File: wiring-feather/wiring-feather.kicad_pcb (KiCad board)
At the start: 2 copper layers, 1 part

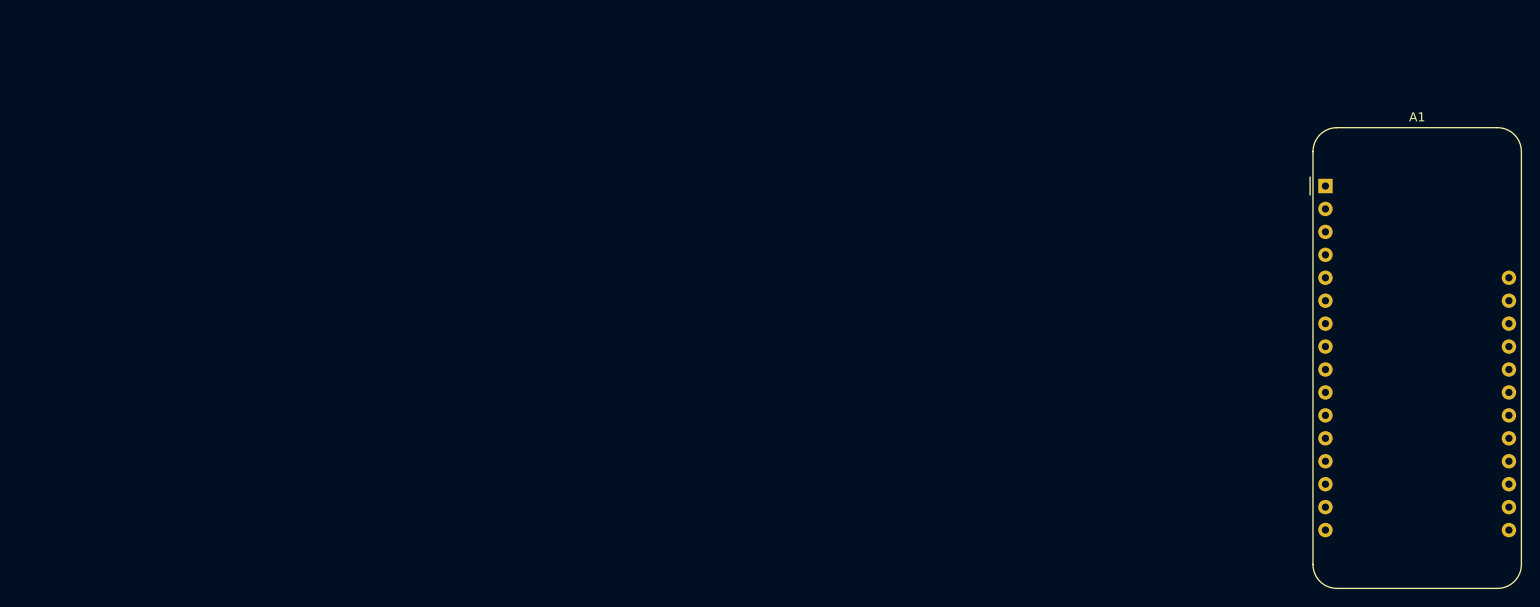
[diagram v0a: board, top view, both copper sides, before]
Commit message: Created footprint for components
All components have footprints, approx for the IMU, auto placed them on the PCB
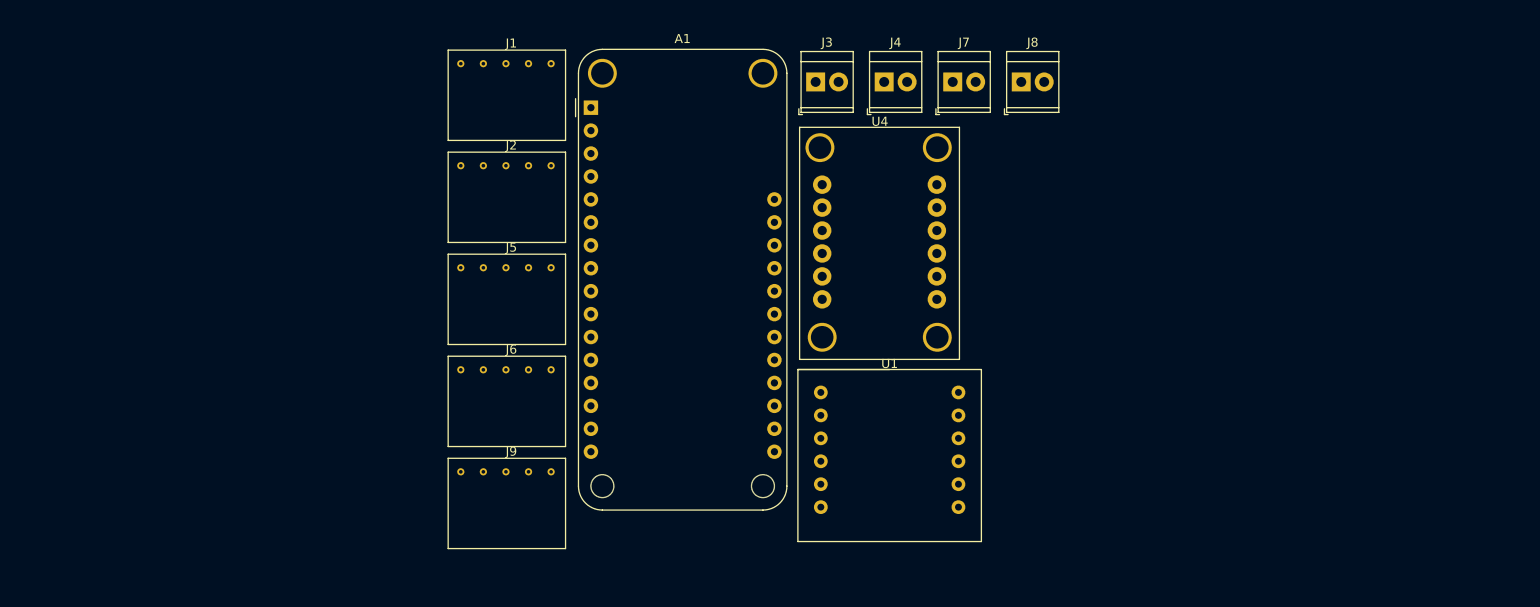
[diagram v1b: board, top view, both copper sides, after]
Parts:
- added J1: M Battery 1, 380_footprint-lib:JST_breakout, F.Cu at (118.8, 66.2)
- added J2: M Battery 1, 380_footprint-lib:JST_breakout, F.Cu at (118.8, 77.5)
- added J3: Screw_Terminal_01x02, 380_footprint-lib:Screw_terminal_TE_Connectivity, F.Cu at (159.4, 69.8)
- added J4: Screw_Terminal_01x02, 380_footprint-lib:Screw_terminal_TE_Connectivity, F.Cu at (167.0, 69.8)
- added J5: JST Breakout Board, 380_footprint-lib:JST_breakout, F.Cu at (118.8, 88.8)
- added J6: JST Breakout Board, 380_footprint-lib:JST_breakout, F.Cu at (118.8, 100.1)
- added J7: Screw_Terminal_01x02, 380_footprint-lib:Screw_terminal_TE_Connectivity, F.Cu at (174.6, 69.8)
- added J8: Screw_Terminal_01x02, 380_footprint-lib:Screw_terminal_TE_Connectivity, F.Cu at (182.2, 69.8)
- added J9: JST Breakout Board, 380_footprint-lib:JST_breakout, F.Cu at (118.8, 111.4)
- added U1: TB6612FNG-Breakout, 380_footprint-lib:DRI0044, F.Cu at (167.6, 104.1)
- added U4: ICM-20948-Adafruit, 380_footprint-lib:ICM-20948, F.Cu at (157.7, 74.8)
- A1: footprint Module:Adafruit_Feather -> 380_footprint-lib:Adafruit_Feather_M0_Adalogger
- moved A1 81.8 mm to (134.6, 72.6)

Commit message: made rough pcb
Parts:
- added D1: D, Connector_PinHeader_2.54mm:PinHeader_1x02_P2.54mm_Vertical, F.Cu at (119.4, 83.8)
- added REF**: MountingHole_2.2mm_M2, MountingHole:MountingHole_2.2mm_M2, F.Cu at (188.0, 118.1)
- added REF**: MountingHole_2.2mm_M2, MountingHole:MountingHole_2.2mm_M2, F.Cu at (102.9, 69.8)
- added REF**: MountingHole_2.2mm_M2, MountingHole:MountingHole_2.2mm_M2, F.Cu at (188.0, 69.8)
- added REF**: MountingHole_2.2mm_M2, MountingHole:MountingHole_2.2mm_M2, F.Cu at (102.9, 118.7)
- J1, J2: footprint 380_footprint-lib:JST_breakout -> Connector_JST:JST_XH_S2B-XH-A_1x02_P2.50mm_Horizontal
- moved J7 73.9 mm to (104.1, 92.1), turned to -90 degrees
- moved J4 65.2 mm to (104.1, 87.0), turned to 90 degrees
- moved U1 34.3 mm to (168.9, 69.8)
- moved J3 33.0 mm to (185.4, 90.2), turned to -90 degrees
- moved J8 29.5 mm to (185.4, 99.1), turned to -90 degrees
- moved J9 22.8 mm to (115.5, 88.9)
- moved J6 18.9 mm to (100.3, 104.1)
- moved J5 15.6 mm to (115.5, 104.1)
- moved U4 15.5 mm to (160.2, 90.1)
- moved J1 12.9 mm to (125.7, 77.1), turned to 180 degrees
- moved J2 3.23 mm to (115.5, 77.1), turned to 180 degrees
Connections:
- A1 pad 19: /PWM-M1 -> /RESET
- A1 pad 20: /DIR1-M1 -> /DIR1-M2
- A1 pad 23: /DIR1-M2 -> /PWM-M1
- A1 pad 24: /RESET -> /DIR1-M1
- J1 pad 1: Net-(D1-K) -> /BATT+
- J1 pad 2: /BATT+ -> Net-(D1-K)
- J2 pad 1: /BATT_ -> Net-(D1-A)
- J2 pad 2: Net-(D1-A) -> /BATT_
- J4 pad 1: /PWR_M2 -> /NEG_M2
- J4 pad 2: /NEG_M2 -> /PWR_M2
- U1 pad 5: unconnected-(U1-GND-Pad5) -> GND
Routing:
- net +3V3: track 0.00 -> 160.4 mm
- net GND: track 0.00 -> 144.4 mm
- net /RESET: track 0.00 -> 89.7 mm
- net /NEG_M2: track 0.00 -> 87.8 mm
- net /PWR_M2: track 0.00 -> 84.5 mm
- net /ENCB_M1: track 0.00 -> 80.6 mm
- net /BATT_: track 0.00 -> 78.0 mm
- net /ENCA_M1: track 0.00 -> 76.2 mm
- net /SDA: track 0.00 -> 72.1 mm
- net /SCL: track 0.00 -> 60.5 mm
- net /BATT+: track 0.00 -> 58.0 mm
- net /INT: track 0.00 -> 49.4 mm
- net /ENCA_M2: track 0.00 -> 33.4 mm
- net /ENCB_M2: track 0.00 -> 32.2 mm
- net /DIR1-M2: track 0.00 -> 28.3 mm
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- added copper zone on F.Cu, net GND
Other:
- board outline added: 92.7 x 55.9 mm

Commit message: updated pcb
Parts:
- J1, J2: footprint Connector_JST:JST_XH_S2B-XH-A_1x02_P2.50mm_Horizontal -> Connector_JST:JST_PH_S2B-PH-K_1x02_P2.00mm_Horizontal
- moved J6 71.2 mm to (171.2, 110.6), turned to 90 degrees
- moved D1 52.3 mm to (171.5, 78.7)
- moved J2 51.8 mm to (167.1, 72.6)
- moved J1 50.2 mm to (175.7, 72.6)
- moved J5 40.7 mm to (156.2, 104.7)
- moved U4 22.9 mm to (137.3, 88.8)
- moved A1 22.9 mm to (111.7, 71.3)
- moved U1 19.1 mm to (149.9, 68.6)
- moved J8 11.2 mm to (177.7, 90.9)
- moved J3 9.92 mm to (177.7, 83.9)
- moved J9 8.98 mm to (109.2, 95.3), turned to -90 degrees
- moved J4 7.22 mm to (104.1, 79.8)
- moved J7 7.22 mm to (104.1, 84.9)
- moved REF** 6.32 mm to (182.0, 116.0)
- moved REF** 6.24 mm to (182.0, 68.0)
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- renumbered REF** to REF
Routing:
- net GND: track 144.4 -> 0.00 mm
- net /BATT_: track 78.0 -> 11.7 mm
- net /RESET: track 89.7 -> 42.0 mm
- net /INT: track 49.4 -> 91.0 mm
- net /ENCA_M1: track 76.2 -> 109.0 mm
- net /BATT+: track 58.0 -> 27.9 mm
- net /ENCB_M1: track 80.6 -> 105.8 mm
- net /ENCA_M2: track 33.4 -> 8.29 mm
- net /ENCB_M2: track 32.2 -> 8.29 mm
- net /NEG_M2: track 87.8 -> 68.2 mm
- net /SCL: track 60.5 -> 79.1 mm
- net /PWR_M2: track 84.5 -> 66.3 mm
- net /SDA_2: track 19.9 -> 4.04 mm
- net /NEG_M1: track 24.9 -> 39.2 mm
- net /SCL_2: track 17.9 -> 4.06 mm
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- added copper zone on B.Cu, net GND
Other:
- board size 92.7 x 55.9 mm -> 89 x 56 mm

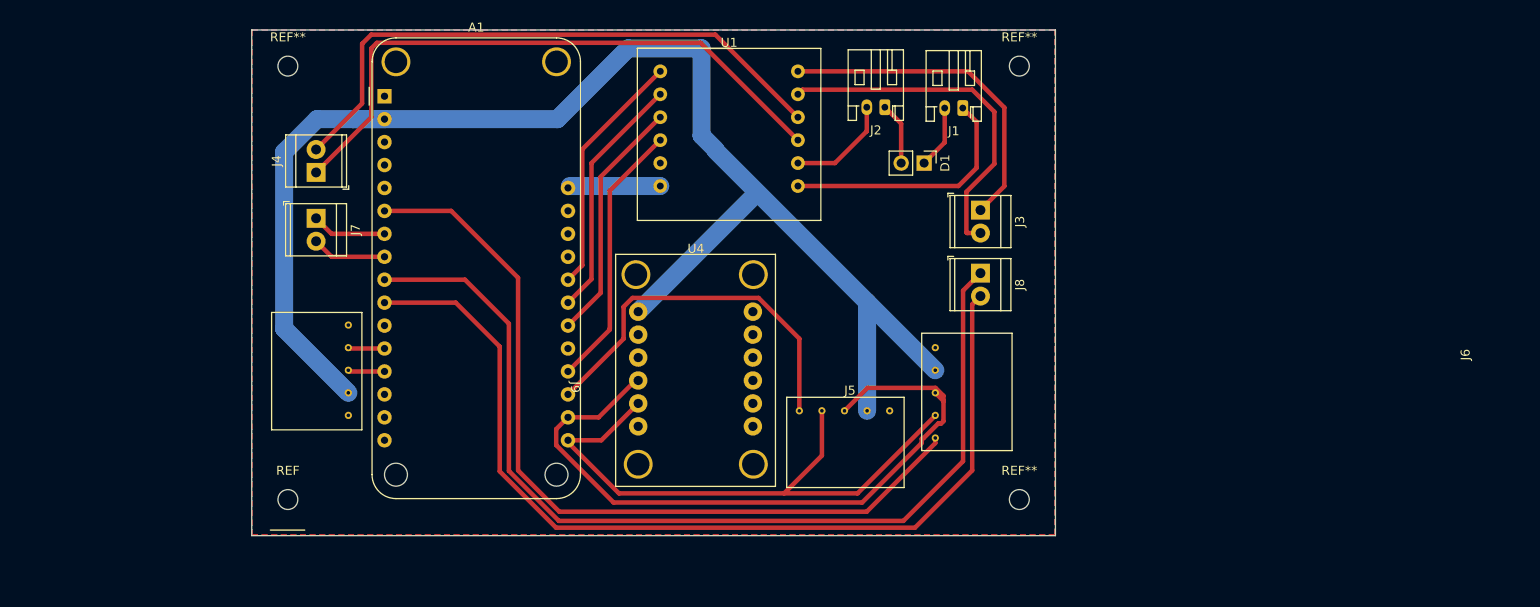
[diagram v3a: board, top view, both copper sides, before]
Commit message: Added testing points, i2c pullup resistors
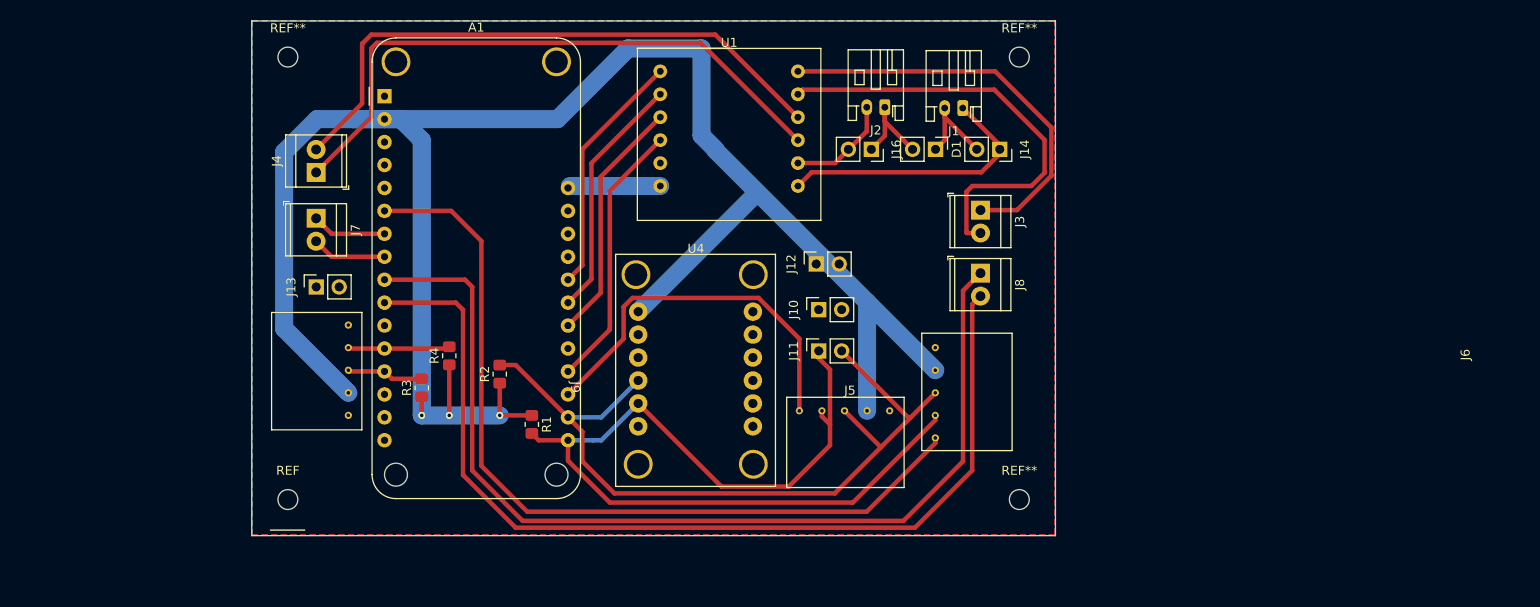
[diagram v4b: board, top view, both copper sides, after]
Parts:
- added J10: GND_TEST, Connector_PinSocket_2.54mm:PinSocket_1x02_P2.54mm_Vertical, F.Cu at (159.8, 95.0)
- added J11: I2C_TEST, Connector_PinSocket_2.54mm:PinSocket_1x02_P2.54mm_Vertical, F.Cu at (159.8, 99.5)
- added J12: 3V3, Connector_PinSocket_2.54mm:PinSocket_1x02_P2.54mm_Vertical, F.Cu at (159.5, 89.9)
- added J13: GND_TEST, Connector_PinSocket_2.54mm:PinSocket_1x02_P2.54mm_Vertical, F.Cu at (104.1, 92.5)
- added J14: BATT2-Charge, Connector_PinSocket_2.54mm:PinSocket_1x02_P2.54mm_Vertical, F.Cu at (179.8, 77.2)
- added J16: BATT1-Charge, Connector_PinSocket_2.54mm:PinSocket_1x02_P2.54mm_Vertical, F.Cu at (165.6, 77.2)
- added R1: 10k, Resistor_SMD:R_0805_2012Metric_Pad1.20x1.40mm_HandSolder, F.Cu at (128.0, 107.7)
- added R2: 10k, Resistor_SMD:R_0805_2012Metric_Pad1.20x1.40mm_HandSolder, F.Cu at (124.5, 102.1)
- added R3: 10k, Resistor_SMD:R_0805_2012Metric_Pad1.20x1.40mm_HandSolder, F.Cu at (115.8, 103.6)
- added R4: 10k, Resistor_SMD:R_0805_2012Metric_Pad1.20x1.40mm_HandSolder, F.Cu at (118.9, 100.1)
- moved D1 1.98 mm to (172.7, 77.2)
- moved REF** 1.00 mm to (101.0, 67.0)
- moved REF** 1.00 mm to (182.0, 67.0)
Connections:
- net /BATT+ renamed /2BATT+
- net /BATT_ renamed /1BATT_
- net Net-(D1-A) renamed /1BATT+
- net Net-(D1-K) renamed /2BATT_
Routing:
- net +3V3: track 161.0 -> 220.0 mm, vias 0 -> 3
- net /SDA: track 67.2 -> 103.3 mm
- net /NEG_M1: track 39.2 -> 49.1 mm
- net /PWR_M1: track 37.0 -> 45.4 mm
- net /SCL: track 79.1 -> 86.5 mm
- net /SDA_2: track 4.04 -> 11.3 mm
- net /SCL_2: track 4.06 -> 8.52 mm
- net /1BATT+: track 6.93 -> 11.2 mm
- net /2BATT_: track 7.04 -> 11.0 mm
- net /2BATT+: track 27.9 -> 31.0 mm
- net /ENCB_M1: track 105.8 -> 108.4 mm
- net /ENCA_M1: track 109.0 -> 111.4 mm
- net /INT: track 91.0 -> 93.1 mm
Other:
- board size 89 x 56 mm -> 89 x 57 mm

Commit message: design checks and silkscreen done
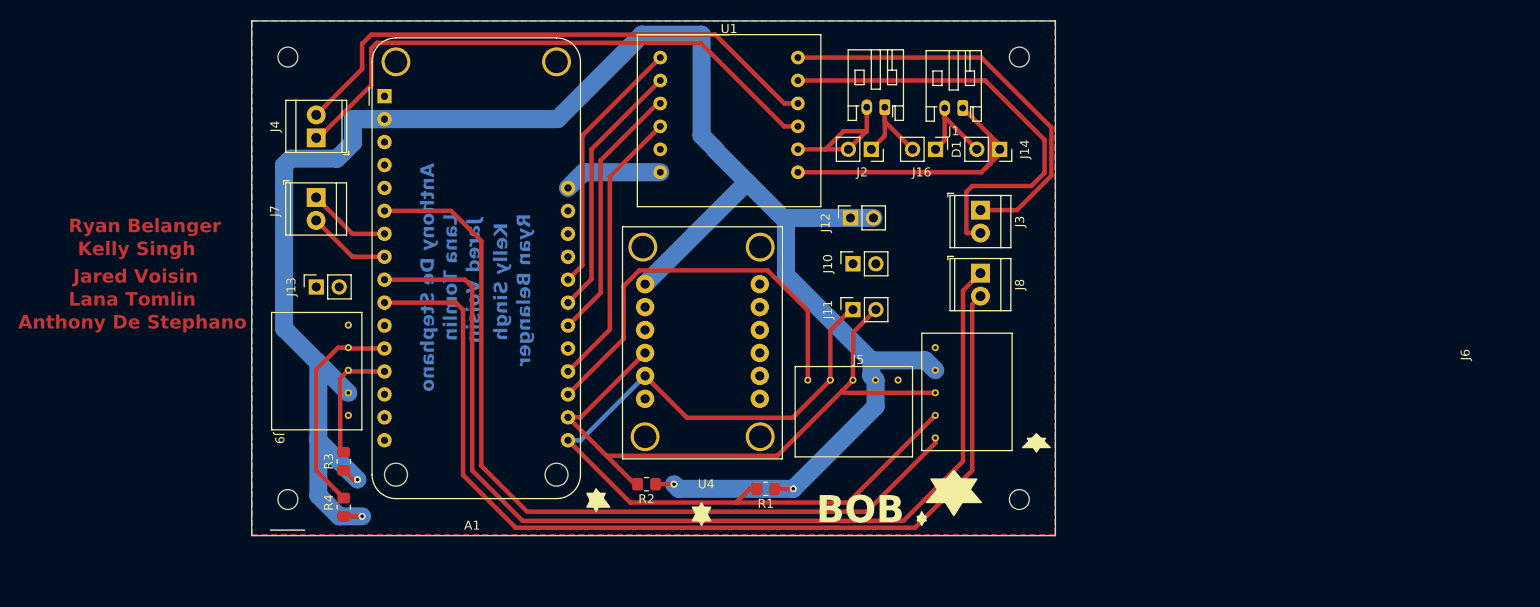
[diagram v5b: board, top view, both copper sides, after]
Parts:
- J13: value GND_TEST -> GND
- J3: value Screw_Terminal_01x02 -> PWR M1
- J5: value JST Breakout Board -> TOF RESET
- J6: value JST Breakout Board -> TOF INT
- J7: value Screw_Terminal_01x02 -> ENC M2
- J8: value Screw_Terminal_01x02 -> ENC M1
- J9: value JST Breakout Board -> TOF DNP [BACK-UP]
- moved R1 26.9 mm to (153.9, 114.8), turned to 180 degrees
- moved R4 20.4 mm to (107.2, 116.8)
- moved R2 20.3 mm to (140.7, 114.3), turned to 180 degrees
- moved R3 11.9 mm to (107.2, 111.8)
- moved J12 6.36 mm to (163.3, 84.8)
- moved J10 6.34 mm to (163.6, 89.9)
- moved J11 5.94 mm to (163.6, 95.0)
- moved J4 3.83 mm to (104.1, 75.9)
- moved J5 3.53 mm to (157.2, 101.3)
- moved U4 3.14 mm to (138.1, 85.8)
- moved J7 2.31 mm to (104.1, 82.5)
- moved U1 1.52 mm to (149.9, 67.1)
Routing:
- net /SCL: track 86.5 -> 72.3 mm
- net /SDA_2: track 11.3 -> 24.1 mm
- net +3V3: track 220.0 -> 229.2 mm, vias 3 -> 4
- net /SDA: track 103.3 -> 95.1 mm
- net /SCL_2: track 8.52 -> 13.7 mm
- net /1BATT_: track 11.7 -> 16.5 mm
- net /PWR_M2: track 66.3 -> 61.8 mm
- net /NEG_M2: track 68.2 -> 63.9 mm
- net /RESET: track 42.0 -> 45.2 mm
- net /2BATT+: track 31.0 -> 33.6 mm
- net /PWM-M2: track 27.3 -> 29.0 mm
- net /PWM-M1: track 27.3 -> 28.8 mm
- net /DIR1-M2: track 29.8 -> 31.4 mm
- net /DIR1-M1: track 27.3 -> 28.8 mm
- net /ENCB_M2: track 8.29 -> 9.24 mm
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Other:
- board text added: "Anthony De Stephano"
- board text added: "BOB"
- board text added: "GND"
- board text added: "I2C"
- board text added: "Jared Voisin"
- board text added: "Kelly Singh"
- board text added: "Lana Tomlin"
- board text added: "Ryan Belanger"
